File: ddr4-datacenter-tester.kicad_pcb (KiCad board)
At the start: 10 copper layers, 152.9 x 90 mm, 304 parts, among them IC1 TPS54561, IC3 TPD8S009DSMR, J1 0878311420, J10 61300311121, J3 DC_SOCKET, J4 WE_629105150521, J6 685119134923, J7 1140084168, J8 61300311121, Q2 BSS138APW, Q3 BSS138APW, Q4 BSS138APW, Q5 BSS138APW, Q6 BSS138APW, Q7 BSS138APW, Q8 BSS138APW, U10 LM3881MME_NOPB, U11 S27KL0641DABHI023, U12 TPS62823DLCT, U14 2199155-1, U15 XC7K160T-FFG676, U3 S25FL128SAGNFI000, U4 TPS65296, U5 TPS62823DLCT, U6 KSZ9031RNXCA, U7 FT4232HQ, U8 SRST, U9 TPS62823DLCT, Y1 ABM8G-25.000MHZ-18-D2Y-T, Y2 ABM8G-12.000MHZ-18-D2Y-T

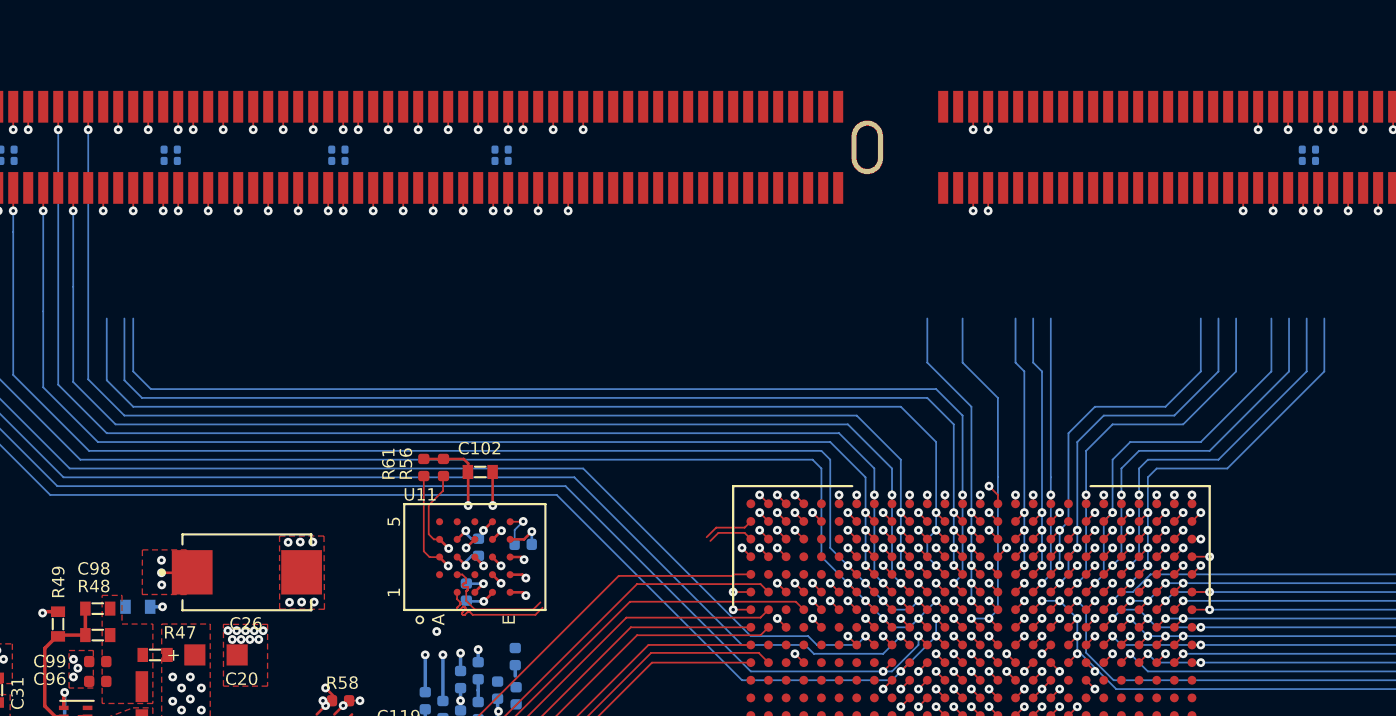
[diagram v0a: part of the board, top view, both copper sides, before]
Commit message: Add ddr4 adress pin routing
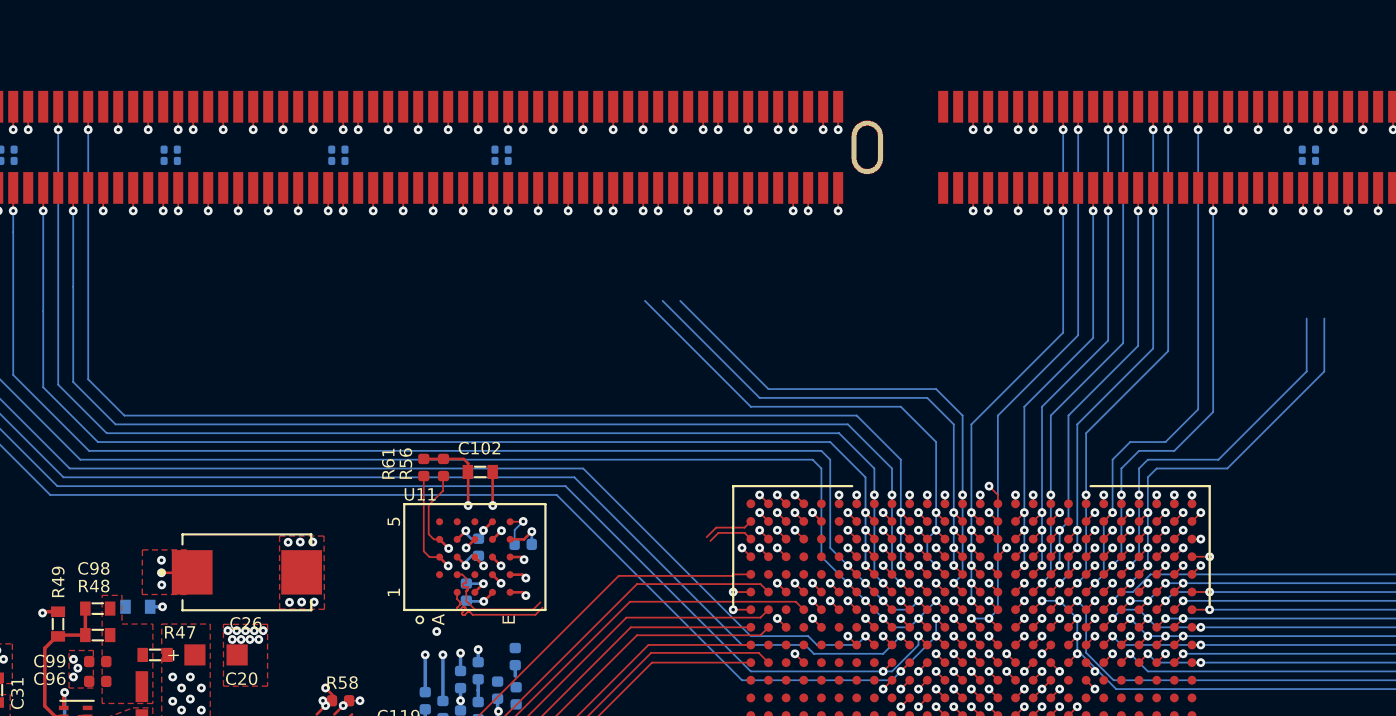
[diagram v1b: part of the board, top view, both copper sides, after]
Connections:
- U15 pad AA10: Net-(U15-PadAA10) -> A12\~BC
- U15 pad AA12: Net-(U15-PadAA12) -> A1
- U15 pad AA7: Net-(U15-PadAA7) -> CKE0
- U15 pad AA8: Net-(U15-PadAA8) -> ~ACT
- U15 pad AA9: Net-(U15-PadAA9) -> BG0
- U15 pad AB10: Net-(U15-PadAB10) -> A9
- U15 pad AB11: Net-(U15-PadAB11) -> A7
- U15 pad AB6: Net-(U15-PadAB6) -> CKE1\NC
- U15 pad AB9: Net-(U15-PadAB9) -> ~ALERT
- U15 pad AD11: Net-(U15-PadAD11) -> ~RESET
- U15 pad AE10: Net-(U15-PadAE10) -> A11
- U15 pad AE11: Net-(U15-PadAE11) -> A2
- U15 pad AF10: Net-(U15-PadAF10) -> A5
- U15 pad AF9: Net-(U15-PadAF9) -> BG1
- U15 pad V12: Net-(U15-PadV12) -> A4
- U15 pad W13: Net-(U15-PadW13) -> A8
- U15 pad Y12: Net-(U15-PadY12) -> A3
- U15 pad Y13: Net-(U15-PadY13) -> A6
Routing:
- net ~RESET: track 0.00 -> 34.8 mm, vias 0 -> 2
- net A8: track 0.00 -> 32.8 mm, vias 0 -> 2
- net Net-(U15-PadAA14): track 61.4 -> 29.1 mm
- net Net-(U15-PadAB15): track 60.1 -> 27.9 mm
- net Net-(U15-PadAB14): track 60.2 -> 28.1 mm
- net CKE0: track 0.00 -> 31.3 mm, vias 0 -> 2
- net A6: track 0.00 -> 30.9 mm, vias 0 -> 2
- net Net-(U15-PadAD11): track 29.9 -> 0.00 mm, vias 1 -> 0
- net BG0: track 0.00 -> 29.9 mm, vias 0 -> 2
- net ~ACT: track 0.00 -> 29.8 mm, vias 0 -> 2
- net A3: track 0.00 -> 29.7 mm, vias 0 -> 2
- net A12\~BC: track 0.00 -> 29.6 mm, vias 0 -> 2
- net A1: track 0.00 -> 28.4 mm, vias 0 -> 2
- net A9: track 0.00 -> 28.3 mm, vias 0 -> 2
- net A4: track 0.00 -> 27.5 mm, vias 0 -> 2
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- added copper zone on VCC1, net 1V8_SYS
- added copper zone on VCC1, net 3V3_SYS
- added copper zone on GND2, net GND
- added copper zone on VCC1, net VDDQ
- removed copper zone on In3_LS.Cu, net (none)
- removed copper zone on In3_LS.Cu, net 1V8_SYS
- removed copper zone on In3_LS.Cu, net 3V3_SYS
- removed copper zone on In2_HS.Cu, net GND
- removed copper zone on In3_LS.Cu, net GND
- removed copper zone on In3_LS.Cu, net VDDQ

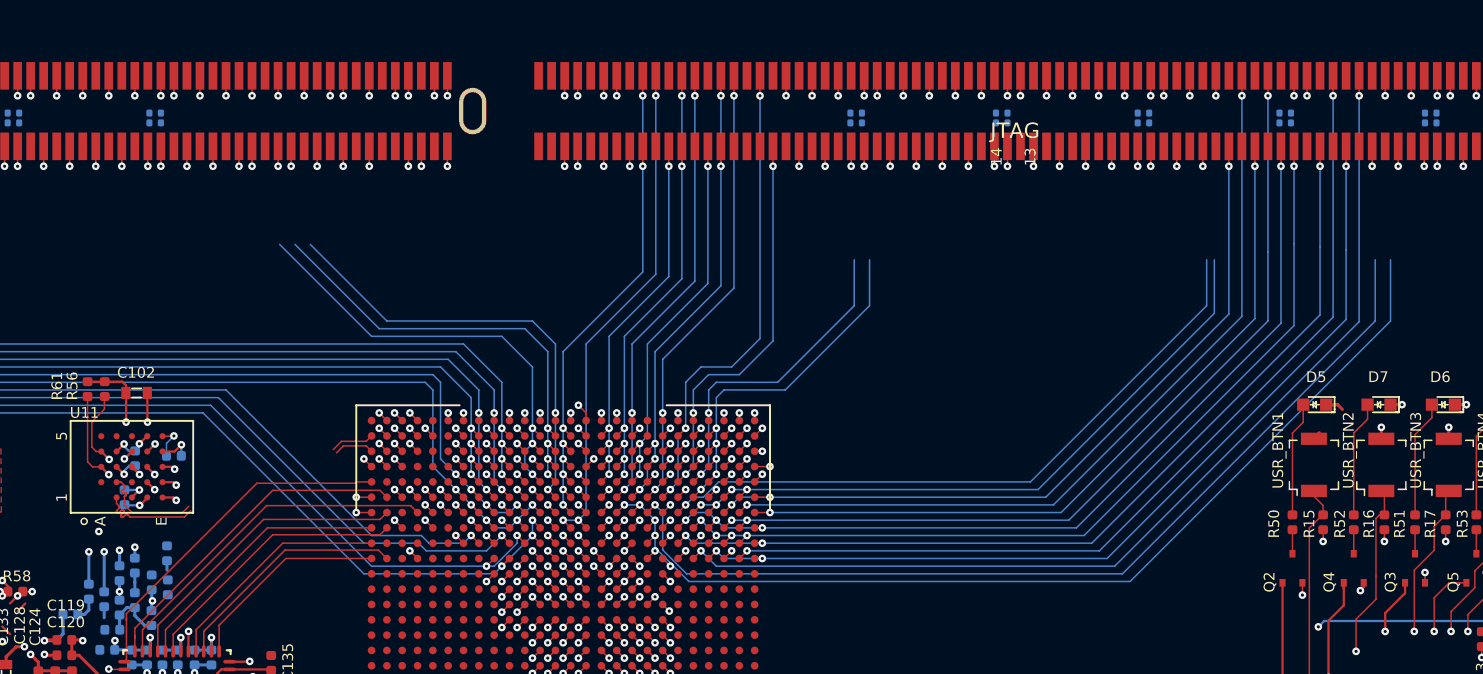
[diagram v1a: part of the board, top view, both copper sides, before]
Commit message: Reroute address pins into bank 33
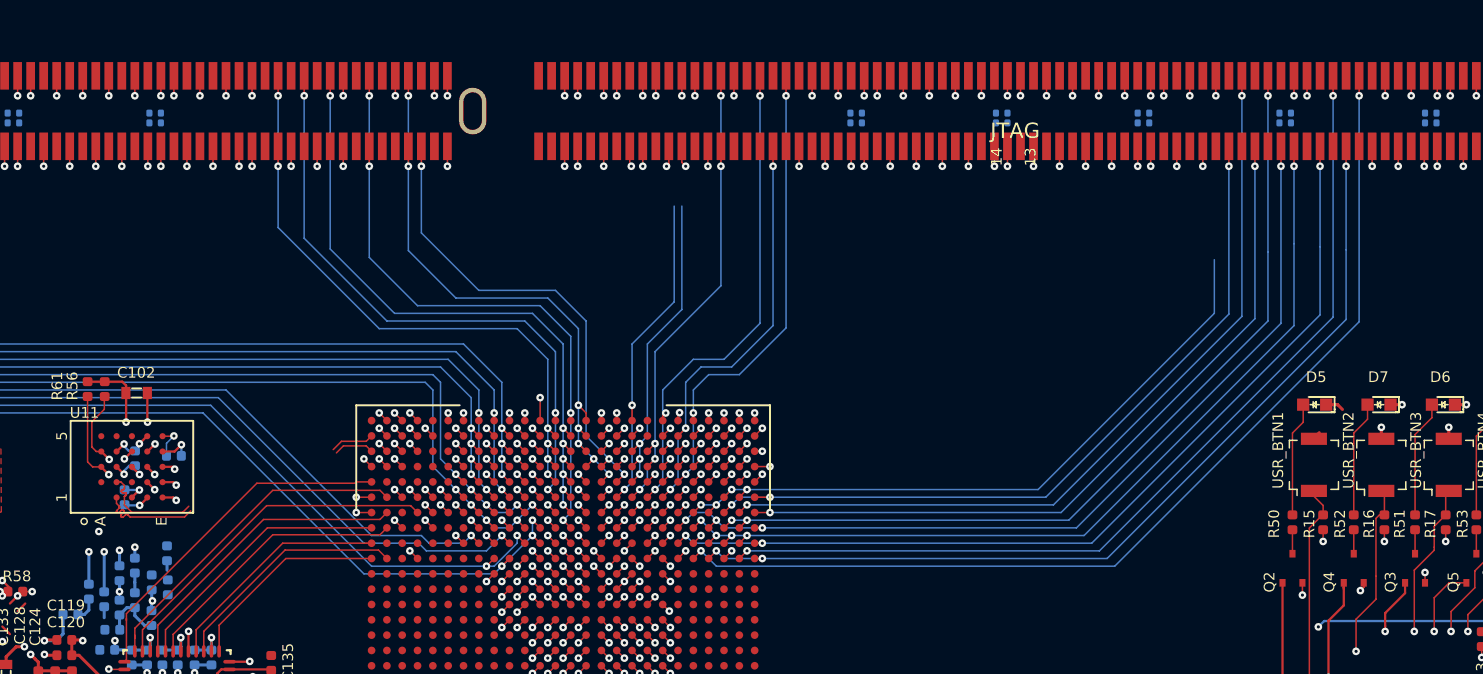
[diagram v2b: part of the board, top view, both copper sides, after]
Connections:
- U15 pad AA10: A12\~BC -> Net-(U15-PadAA10)
- U15 pad AA12: A1 -> ~RAS~\A16
- U15 pad AA13: Net-(U15-PadAA13) -> ~WE~\A14
- U15 pad AA14: Net-(U15-PadAA14) -> ~CS1~\NC
- U15 pad AA3: Net-(U15-PadAA3) -> DQ25
- U15 pad AA5: Net-(U15-PadAA5) -> DQS3_T
- U15 pad AA7: CKE0 -> CKE1\NC
- U15 pad AA8: ~ACT -> CKE0
- U15 pad AB10: A9 -> BA1
- U15 pad AB11: A7 -> BA0
- U15 pad AB14: Net-(U15-PadAB14) -> ODT1\NC
- U15 pad AB15: Net-(U15-PadAB15) -> DQ36
- U15 pad AB4: Net-(U15-PadAB4) -> DQ30
- U15 pad AB5: Net-(U15-PadAB5) -> DQS3_C
- U15 pad AB6: CKE1\NC -> ~RESET
- U15 pad AB7: DQ28 -> A12\~BC
- U15 pad AB9: ~ALERT -> Net-(U15-PadAB9)
- U15 pad AC11: DQ27 -> A1
- U15 pad AC13: Net-(U15-PadAC13) -> A17
- U15 pad AC14: Net-(U15-PadAC14) -> ~CS2~\C0
- U15 pad AC3: Net-(U15-PadAC3) -> DQ31
- U15 pad AC4: Net-(U15-PadAC4) -> DQ27
- U15 pad AC7: DQ29 -> A11
- U15 pad AC8: DQS3_T -> A6
- U15 pad AC9: DQ31 -> A4
- U15 pad AD10: DQ26 -> A3
- U15 pad AD11: ~RESET -> A2
- U15 pad AD13: Net-(U15-PadAD13) -> A13
- U15 pad AD14: Net-(U15-PadAD14) -> NC\C2
- U15 pad AD15: DQ36 -> Net-(U15-PadAD15)
- U15 pad AD3: Net-(U15-PadAD3) -> DQ26
- U15 pad AD8: DQS3_C -> A8
- U15 pad AD9: DQ30 -> A5
- U15 pad AE10: A11 -> ~ALERT
- U15 pad AE11: A2 -> Net-(U15-PadAE11)
- U15 pad AE13: Net-(U15-PadAE13) -> PARITY
- U15 pad AE7: DQ24 -> A9
- U15 pad AF10: A5 -> Net-(U15-PadAF10)
- U15 pad AF13: Net-(U15-PadAF13) -> ~CAS~\A15
- U15 pad AF14: Net-(U15-PadAF14) -> ~EVENT
- U15 pad AF15: Net-(U15-PadAF15) -> ~CS3~\C1,NC
- U15 pad AF7: DQ25 -> A7
- U15 pad V12: A4 -> A0
- U15 pad V13: Net-(U15-PadV13) -> SA2
- U15 pad V3: Net-(U15-PadV3) -> DQ28
- U15 pad V4: Net-(U15-PadV4) -> DQ29
- U15 pad W13: A8 -> ~CS0
- U15 pad W4: Net-(U15-PadW4) -> DQ24
- U15 pad Y10: Net-(U15-PadY10) -> ~SAVE
- U15 pad Y12: A3 -> A10\AP
- U15 pad Y13: A6 -> ODT0
- U15 pad Y8: Net-(U15-PadY8) -> ~ACT
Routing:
- net Net-(U15-PadY10): track 64.9 -> 0.00 mm, vias 1 -> 0
- net Net-(U15-PadY8): track 61.8 -> 0.00 mm, vias 1 -> 0
- net Net-(U15-PadV4): track 45.6 -> 0.00 mm, vias 1 -> 0
- net Net-(U15-PadV3): track 45.6 -> 0.00 mm, vias 1 -> 0
- net Net-(U15-PadW4): track 44.6 -> 0.00 mm, vias 1 -> 0
- net Net-(U15-PadY6): track 43.1 -> 0.71 mm
- net Net-(U15-PadAA4): track 41.5 -> 0.00 mm, vias 1 -> 0
- net SA2: track 1.30 -> 42.7 mm, vias 1 -> 2
- net Net-(U15-PadAA3): track 41.4 -> 0.00 mm, vias 1 -> 0
- net Net-(U15-PadAB4): track 40.1 -> 0.00 mm, vias 1 -> 0
- net ODT0: track 1.30 -> 40.3 mm, vias 1 -> 2
- net ~CS0: track 1.30 -> 40.0 mm, vias 1 -> 2
- net ~CS1~\NC: track 1.30 -> 40.0 mm, vias 1 -> 2
- net ~CS2~\C0: track 1.30 -> 39.6 mm, vias 1 -> 2
- net A0: track 1.30 -> 39.4 mm, vias 1 -> 2
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
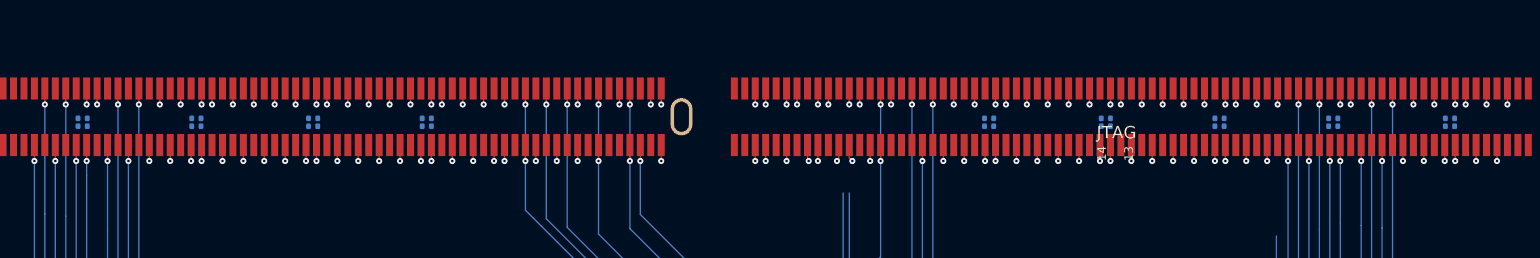
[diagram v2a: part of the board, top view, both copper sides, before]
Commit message: Add DQS[9:17] routing through 0R
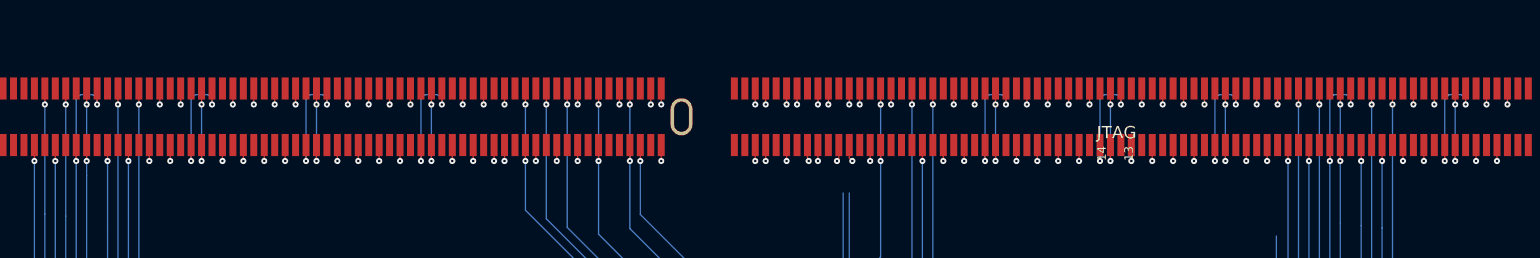
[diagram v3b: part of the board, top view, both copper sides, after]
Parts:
- moved R100 1.86 mm to (231.3, 59.7)
- moved R107 1.86 mm to (147.2, 59.7)
- moved R111 1.86 mm to (128.5, 59.7)
- moved R114 1.86 mm to (203.3, 59.7), turned to 270 degrees
- moved R102 1.85 mm to (222.0, 59.7), turned to 270 degrees
- moved R103 1.85 mm to (211.8, 59.7)
- moved R105 1.85 mm to (156.5, 59.7)
- moved R108 1.85 mm to (148.0, 59.7)
- moved R99 1.85 mm to (230.5, 59.7)
- moved R110 1.85 mm to (138.7, 59.7)
- moved R113 1.85 mm to (202.4, 59.7)
- moved R98 1.85 mm to (240.7, 59.7)
- moved R109 1.85 mm to (137.8, 59.7)
- moved R112 1.85 mm to (129.3, 59.7)
- moved R97 1.85 mm to (239.8, 59.7)
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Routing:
- net DQS16_T: track 1.30 -> 7.17 mm
- net DQS11_T: track 1.30 -> 7.17 mm
- net DQS10_T: track 1.30 -> 7.17 mm
- net DQS9_T: track 1.30 -> 7.17 mm
- net DQS17_T: track 1.30 -> 7.17 mm
- net DQS15_T: track 1.30 -> 7.17 mm
- net DQS14_T: track 1.30 -> 7.17 mm
- net DQS13_T: track 1.30 -> 7.17 mm
- net DQS12_T: track 1.30 -> 7.17 mm
- net DQS9_C: track 1.30 -> 4.33 mm
- net DQS17_C: track 1.30 -> 4.33 mm
- net DQS16_C: track 1.30 -> 4.33 mm
- net DQS15_C: track 1.30 -> 4.33 mm
- net DQS14_C: track 1.30 -> 4.33 mm
- net DQS13_C: track 1.30 -> 4.33 mm
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
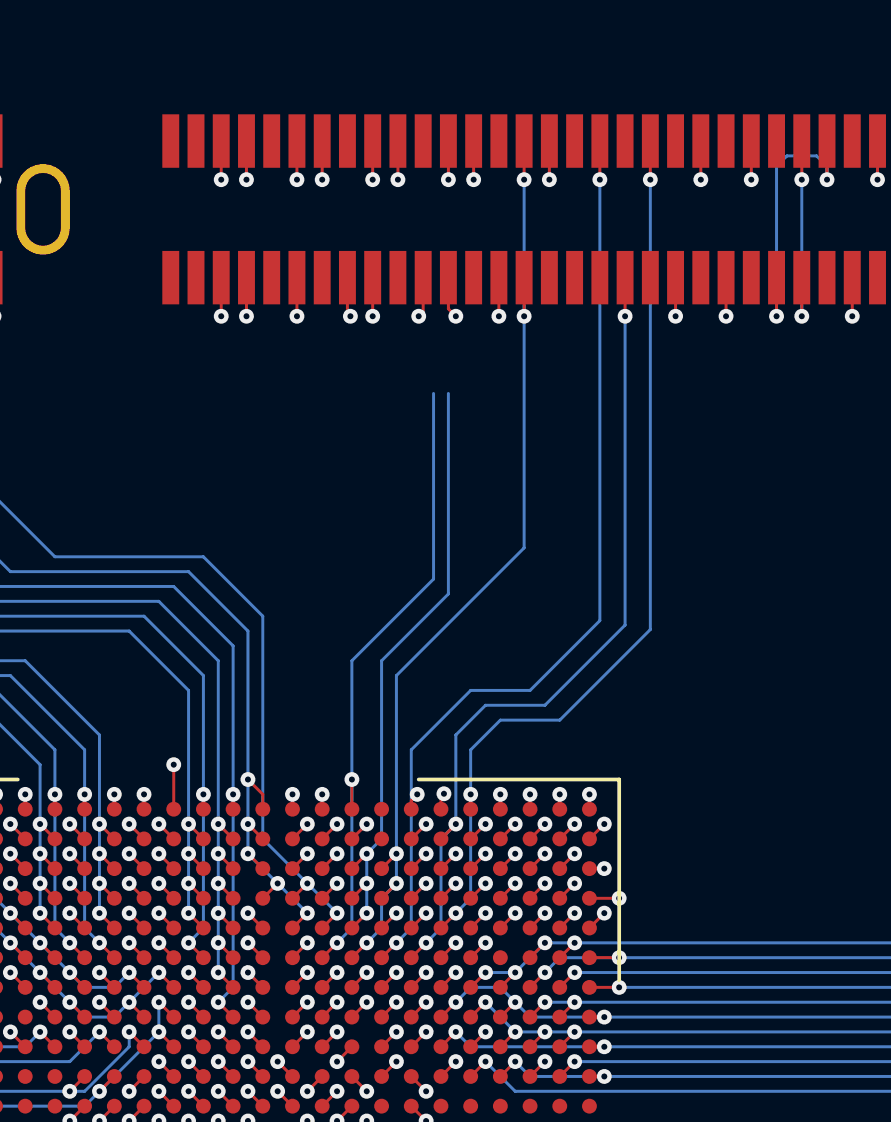
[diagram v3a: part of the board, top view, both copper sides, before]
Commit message: Remap address pins to release DQS pair
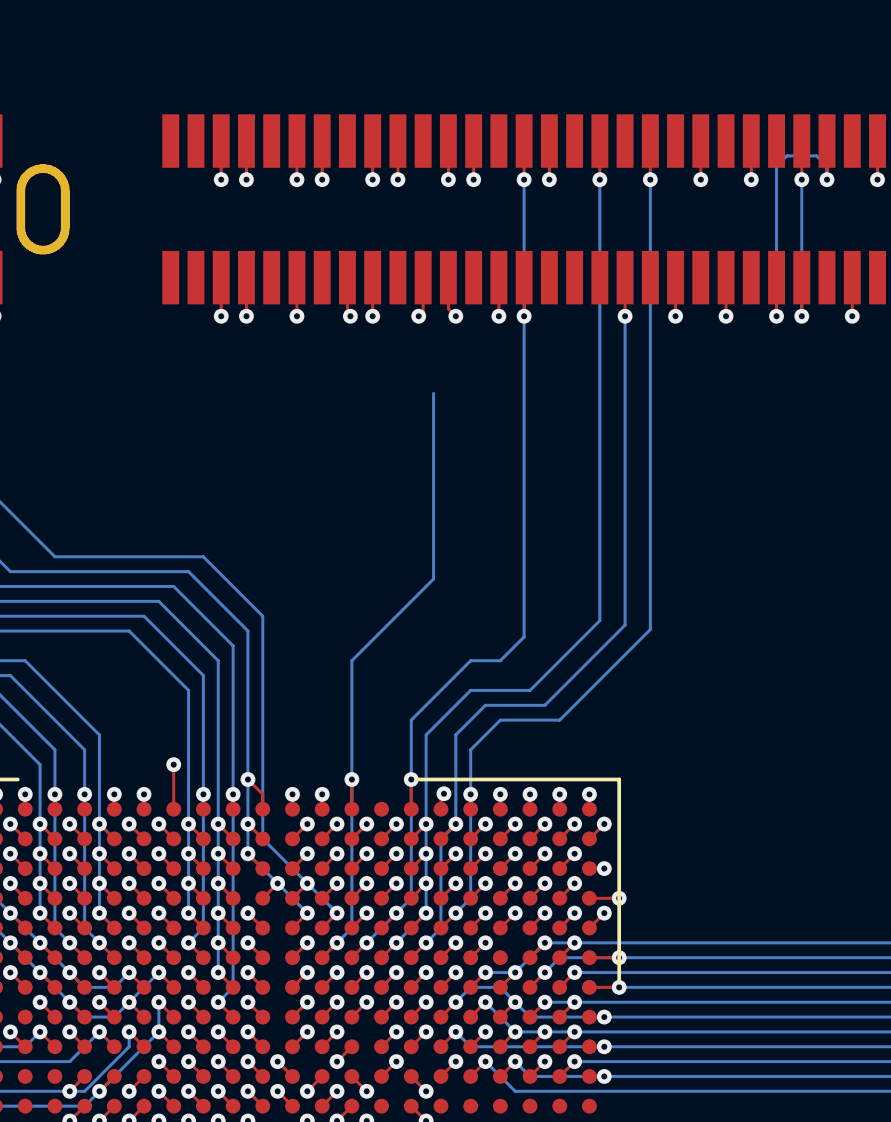
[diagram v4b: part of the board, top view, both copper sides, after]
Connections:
- U15 pad AB9: Net-(U15-PadAB9) -> A6
- U15 pad AC8: A6 -> Net-(U15-PadAC8)
- U15 pad AD8: A8 -> Net-(U15-PadAD8)
- U15 pad AE8: Net-(U15-PadAE8) -> A8
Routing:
- net Net-(U15-PadAB9): track 19.3 -> 0.00 mm, vias 1 -> 0
- net CB3: track 28.8 -> 30.5 mm
- net CB2: track 32.5 -> 33.6 mm
- net A8: track 24.9 -> 23.9 mm
- net A6: track 26.2 -> 27.2 mm
- net Net-(U15-PadAD8): track 0.00 -> 0.71 mm, vias 0 -> 1
- net Net-(U15-PadAC8): track 0.00 -> 0.71 mm, vias 0 -> 1
- net BG0: track 29.9 -> 30.5 mm
